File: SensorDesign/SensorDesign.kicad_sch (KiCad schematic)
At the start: 8 parts, among them Q1 BC557, SW1 SW_Mouse, U1 LM358

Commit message: Update circuit.
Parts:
- removed D1, D2: 1N4148, symbol Device:D
- removed Q1: BC557, symbol Device:Q_PNP_CBE
- removed R2: 6.8k, symbol Device:R_US
- removed R3: 2.2k, symbol Device:R_US
- added C1: 100u, symbol Device:C_Polarized_US
- added unit 2 of U1
- R1: value 2.2k -> 1k
- U1: value LM358 -> TLC272
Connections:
- net 0.23V is gone; now on net A0: U1.2 (-)
- net AmbientSensor_Out: now also U1.5 (+); no longer U1.3 (+)
- net Arduino_GND: now also C1.2; no longer R1.2
- net A0: now reaches R1.1
- net A0: now also C1.1
- new net A1: U1.3 (+), U1.6 (-), U1.7
- new net Arduino_3: R1.2
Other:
- moved on the sheet: SW1, U1A, U1C

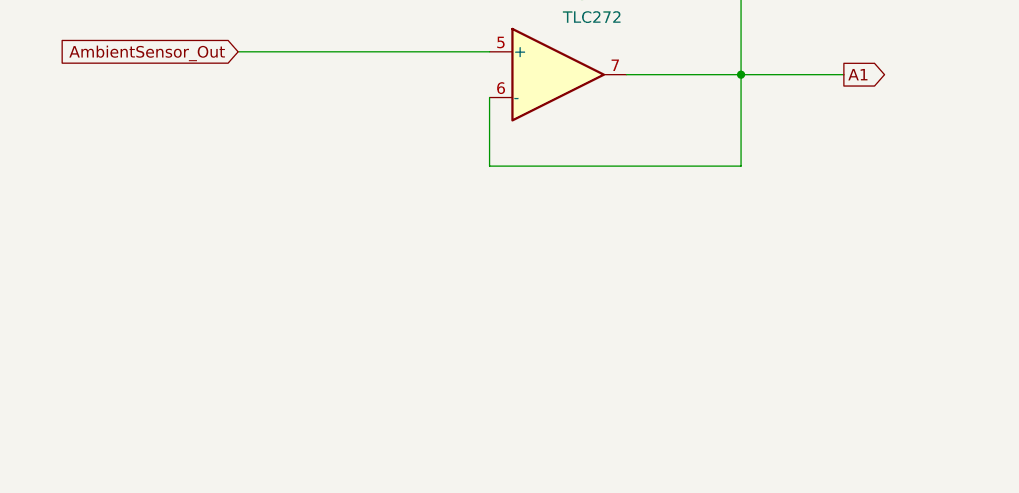
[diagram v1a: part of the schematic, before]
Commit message: Add Edge trigger mode.
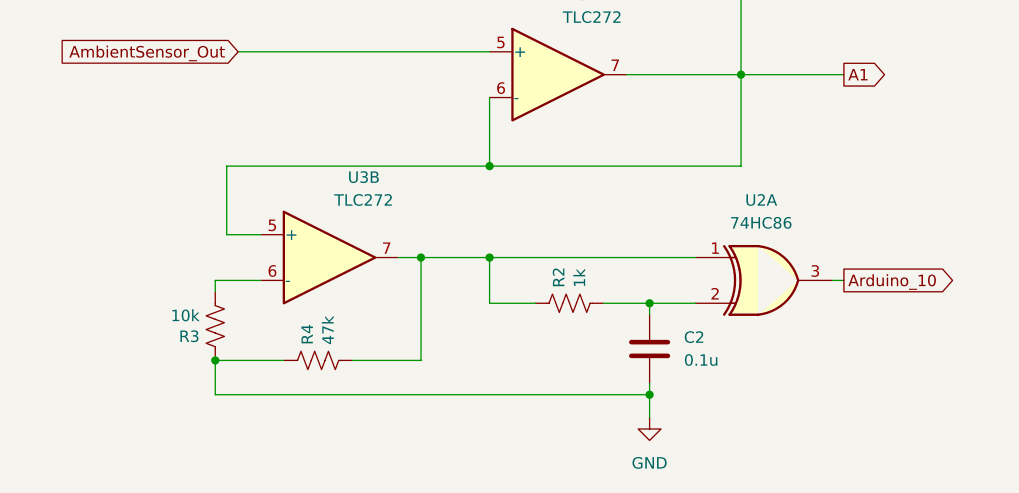
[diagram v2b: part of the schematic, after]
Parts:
- added C2: 0.1u, symbol Device:C
- added R2: 1k, symbol Device:R_US
- added R3: 10k, symbol Device:R_US
- added R4: 47k, symbol Device:R_US
- added U2: 74HC86, symbol 74xx:74HC86
- added U3: TLC272, symbol Amplifier_Operational:LM358
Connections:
- net A1: now also U3.5 (+)
- new net: R3.2, U3.6 (-)
- new net: R2.1, R4.2, U2.1, U3.7
- new net: C2.1, R2.2, U2.2
- new net Arduino_10: U2.3
- new net GND: C2.2, R3.1, R4.1
